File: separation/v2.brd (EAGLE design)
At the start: 40.6 x 27.9 mm, 18 parts, among them Q1 IRLZ24NPBF

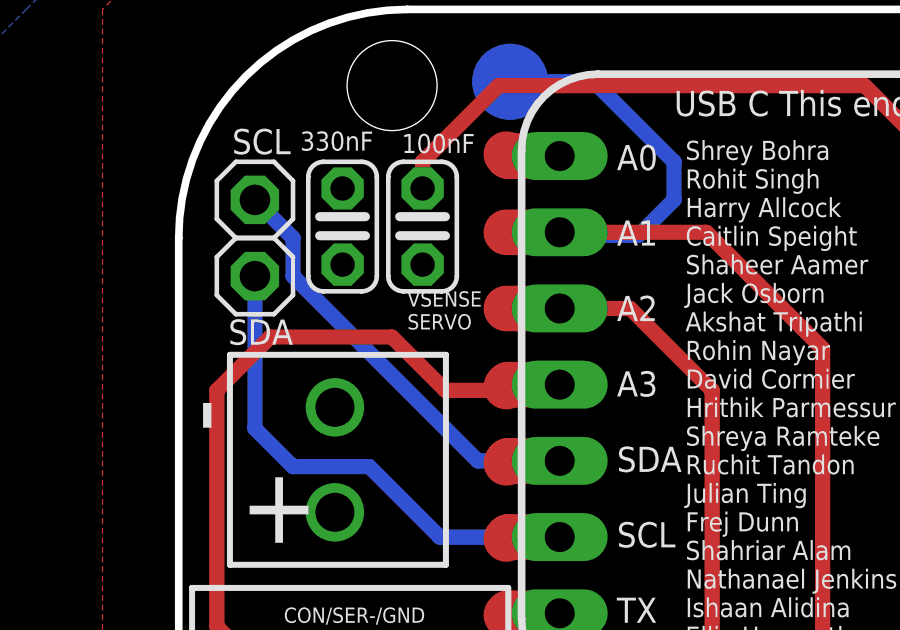
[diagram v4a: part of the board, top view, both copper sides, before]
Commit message: increase pour isolate
now 0.01
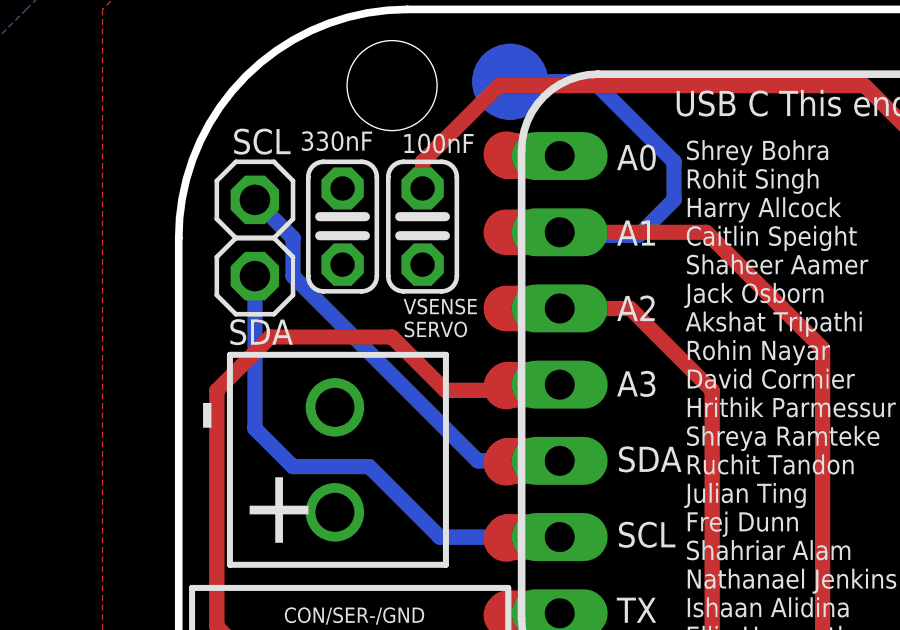
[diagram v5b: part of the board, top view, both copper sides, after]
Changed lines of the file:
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@@
 <text x="-20.193" y="7.747" size="2.54" layer="22" font="vector" rot="MR90">+</text>
 <text x="-20.447" y="11.303" size="2.54" layer="22" font="vector" rot="MR90">-</text>
-<text x="-12.7" y="14.732" size="0.508" layer="21" font="vector">VSENSE
+<text x="-12.827" y="14.478" size="0.508" layer="21" font="vector">VSENSE
 SERVO</text>
 <text x="-18.542" y="20.574" size="0.8382" layer="21" font="vector">SCL</text>
@@
 <text x="18.796" y="16.256" size="0.8382" layer="22" font="vector" rot="MR90">GND</text>
 <text x="16.51" y="21.59" size="0.8382" layer="21" font="vector">VCC</text>
-<text x="6.35" y="1.27" size="1.27" layer="22" font="vector" ratio="12" rot="MR0">ART Separation</text>
+<text x="6.35" y="2.159" size="1.27" layer="22" font="vector" ratio="12" rot="MR0">ART Separation</text>
 <text x="-4.318" y="3.048" size="0.8382" layer="21" font="vector">STEMMA this end</text>
 <text x="-3.81" y="21.844" size="0.8382" layer="21" font="vector">USB C This end</text>
@@
 <contactref element="Q1" pad="3"/>
 <contactref element="R3" pad="2"/>
-<polygon width="0.508" layer="16">
+<polygon width="0.508" layer="16" isolate="0.254">
 <vertex x="-25.4" y="25.4"/>
 <vertex x="-20.32" y="30.48"/>
@@
 <vertex x="-26.67" y="24.13"/>
 </polygon>
+<wire x1="-15.113" y1="12.136" x2="-14.859" y2="16.891" width="0" layer="19" extent="1-1"/>
 </signal>
 <signal name="MOSI">
@@
 <contactref element="C2" pad="2"/>
 <wire x1="-1.397" y1="0.254" x2="-1.524" y2="0.254" width="1.016" layer="1"/>
-<polygon width="0.508" layer="1">
+<polygon width="0.508" layer="1" isolate="0.254">
 <vertex x="-20.32" y="27.94"/>
 <vertex x="-22.86" y="25.4"/>
@@
 <vertex x="12.7" y="27.94"/>
 </polygon>
+<wire x1="-1.397" y1="0.254" x2="14.224" y2="14.605" width="0" layer="19" extent="1-1"/>
+<wire x1="-7.62" y1="0" x2="-1.524" y2="0.254" width="0" layer="19" extent="1-1"/>
+<wire x1="-15.113" y1="8.636" x2="-7.62" y2="0" width="0" layer="19" extent="1-1"/>
+<wire x1="-14.859" y1="19.431" x2="-15.113" y2="8.636" width="0" layer="19" extent="1-1"/>
 </signal>
 <signal name="SERVO">

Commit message: drc check
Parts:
- moved TP2 29.1 mm to (10.2, 1.27)
- moved C1 0.65 mm to (-12.1, 17.5)
- moved C2 0.65 mm to (-14.7, 17.5), turned to 270 degrees
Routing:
- net SERPOW: track 28.5 -> 22.4 mm, vias 0 -> 1
- net VSENSE: track 42.3 -> 37.2 mm
- net SERVO: track 21.7 -> 18.9 mm
- net SCL: track 18.5 -> 17.1 mm
- net SDA: track 16.3 -> 17.1 mm

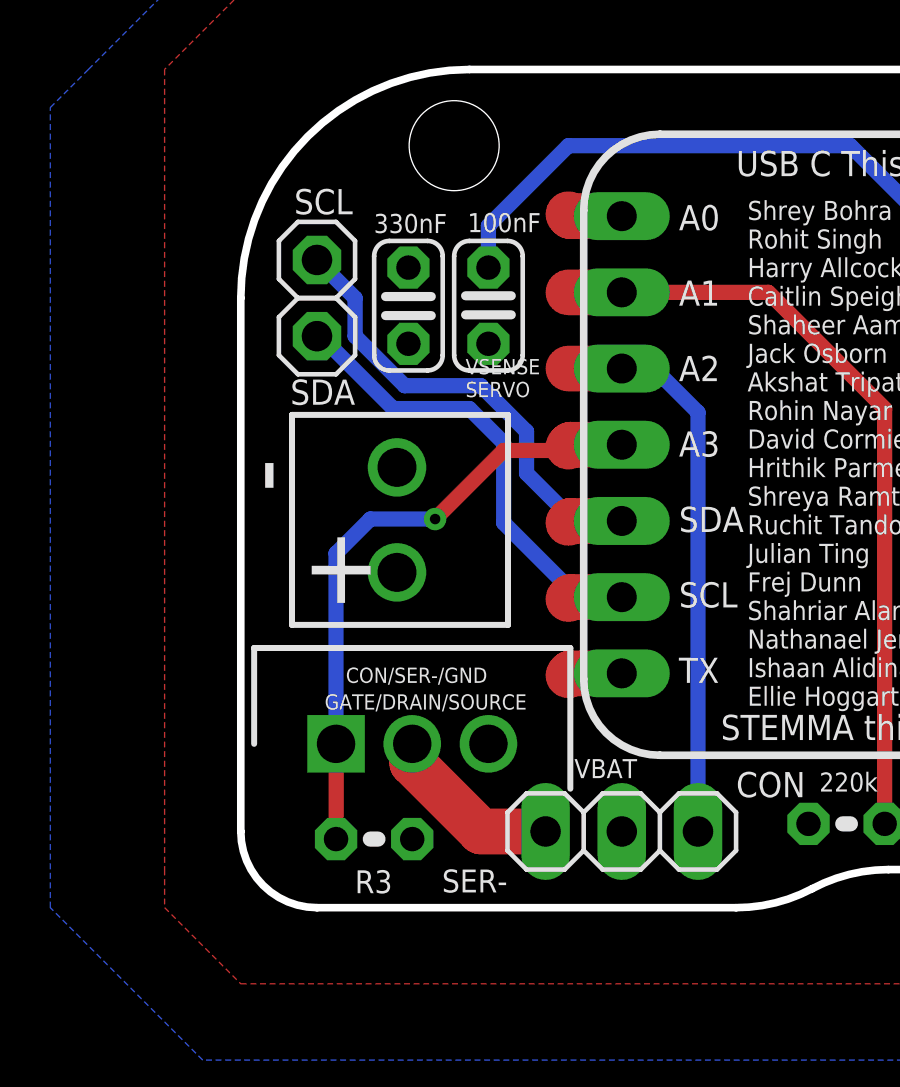
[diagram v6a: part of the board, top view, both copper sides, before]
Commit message: consistent orientation for caps
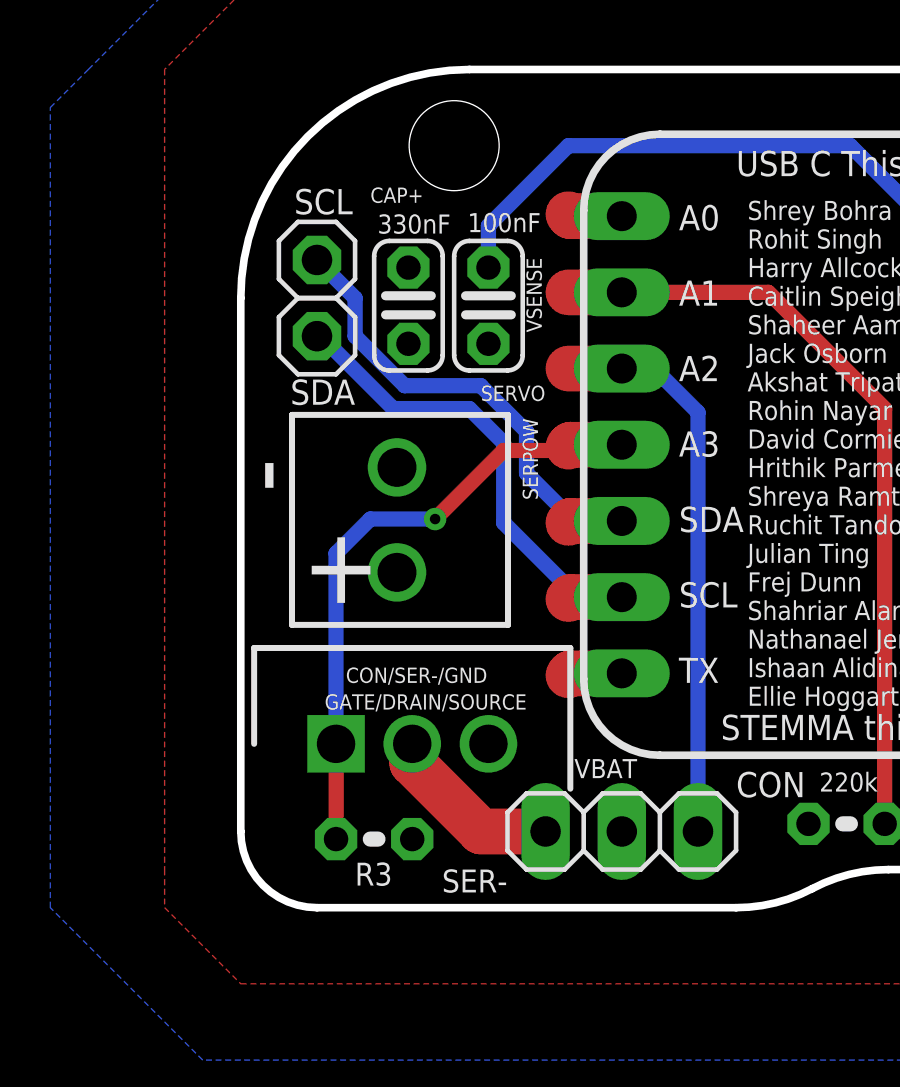
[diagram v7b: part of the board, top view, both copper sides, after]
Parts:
- turned C2 to 90 degrees
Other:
- board text added: "CAP+"
- board text added: "SERPOW"
- board text added: "SERVO"
- board text removed: "VSENSE SERVO"
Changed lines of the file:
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@@
 <text x="-20.193" y="7.747" size="2.54" layer="22" font="vector" rot="MR90">+</text>
 <text x="-20.447" y="11.303" size="2.54" layer="22" font="vector" rot="MR90">-</text>
-<text x="-12.827" y="14.478" size="0.508" layer="21" font="vector">VSENSE
-SERVO</text>
+<text x="-12.319" y="14.351" size="0.508" layer="21" font="vector">SERVO</text>
 <text x="-18.542" y="20.574" size="0.8382" layer="21" font="vector">SCL</text>
 <text x="-18.669" y="14.224" size="0.8382" layer="21" font="vector">SDA</text>
@@
 <text x="-17.526" y="4.064" size="0.508" layer="21" font="vector" ratio="12">GATE/DRAIN/SOURCE</text>
 <text x="-17.018" y="4.953" size="0.508" layer="21" font="vector" ratio="14"> CON/SER-/GND</text>
+<text x="-16.002" y="20.955" size="0.508" layer="21" font="vector" ratio="12">CAP+</text>
+<text x="-10.414" y="11.049" size="0.508" layer="21" font="vector" ratio="12" rot="R90">SERPOW</text>
+<text x="-10.287" y="16.637" size="0.508" layer="21" font="vector" ratio="12" rot="R90">VSENSE</text>
+<text x="11.684" y="0.127" size="0.508" layer="22" font="vector" ratio="12" rot="MR180">VSENSE</text>
 </plain>
 <attributes>
@@
 <attribute name="VALUE" x="-12.7616375" y="19.97729375" size="0.635" layer="21" font="vector" ratio="10"/>
 </element>
-<element name="C2" library="rcl" library_urn="urn:adsk.eagle:library:334" package="C025-024X044" package3d_urn="urn:adsk.eagle:package:23630/1" value="330nF" x="-14.732" y="17.526" smashed="yes" rot="R270">
-<attribute name="POPULARITY" value="56" x="-14.732" y="17.526" size="1.778" layer="27" rot="R270" display="off"/>
-<attribute name="SPICEPREFIX" value="C" x="-14.732" y="17.526" size="1.778" layer="27" rot="R270" display="off"/>
-<attribute name="VALUE" x="-13.443946875" y="20.583021875" size="0.635" layer="21" font="vector" ratio="10" rot="R180"/>
+<element name="C2" library="rcl" library_urn="urn:adsk.eagle:library:334" package="C025-024X044" package3d_urn="urn:adsk.eagle:package:23630/1" value="330nF" x="-14.732" y="17.526" smashed="yes" rot="R90">
+<attribute name="POPULARITY" value="56" x="-14.732" y="17.526" size="1.778" layer="27" rot="R90" display="off"/>
+<attribute name="SPICEPREFIX" value="C" x="-14.732" y="17.526" size="1.778" layer="27" rot="R90" display="off"/>
+<attribute name="VALUE" x="-15.766053125" y="19.929978125" size="0.635" layer="21" font="vector" ratio="10"/>
 </element>
 <element name="Q1" library="SamacSys_Parts" package="TO254P469X1042X1967-3P" value="IRLZ24NPBF" x="-17.145" y="2.921" smashed="yes">
@@
 </element>
 <element name="R3" library="rcl" library_urn="urn:adsk.eagle:library:334" package="0204V" package3d_urn="urn:adsk.eagle:package:23495/1" value="" x="-15.875" y="-0.254" smashed="yes">
-<attribute name="NAME" x="-15.2654" y="-1.2954" size="0.762" layer="25" ratio="10" rot="R180"/>
+<attribute name="NAME" x="-15.2654" y="-1.0414" size="0.762" layer="25" ratio="10" rot="R180"/>
 <attribute name="POPULARITY" value="11" x="-15.875" y="-0.254" size="1.778" layer="27" display="off"/>
 <attribute name="SPICEPREFIX" value="R" x="-15.875" y="-0.254" size="1.778" layer="27" display="off"/>
